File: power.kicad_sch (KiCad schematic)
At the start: 55 parts, among them J3 Conn_02x02_Counter_Clockwise, Q3 Q_NMOS, Q4 Q_NMOS, Q5 Q_NMOS, Q6 Q_NMOS, U10 CJ431, U6 TPS5430DDA, U7 TPS56A37, U8 TPS2121, U9 LDL212PV33R

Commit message: schem: add title
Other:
- company: (none) -> Rémi Ait-Younes
- title: (none) -> Motor Power POC
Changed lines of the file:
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@@
 	(generator_version "9.0")
 	(paper "A4")
+	(title_block
+		(title "Motor Power POC")
+		(date "2025-11-30")
+		(rev "01")
+		(company "Rémi Ait-Younes")
+	)
 	(rectangle
 		(start 246.38 93.98)

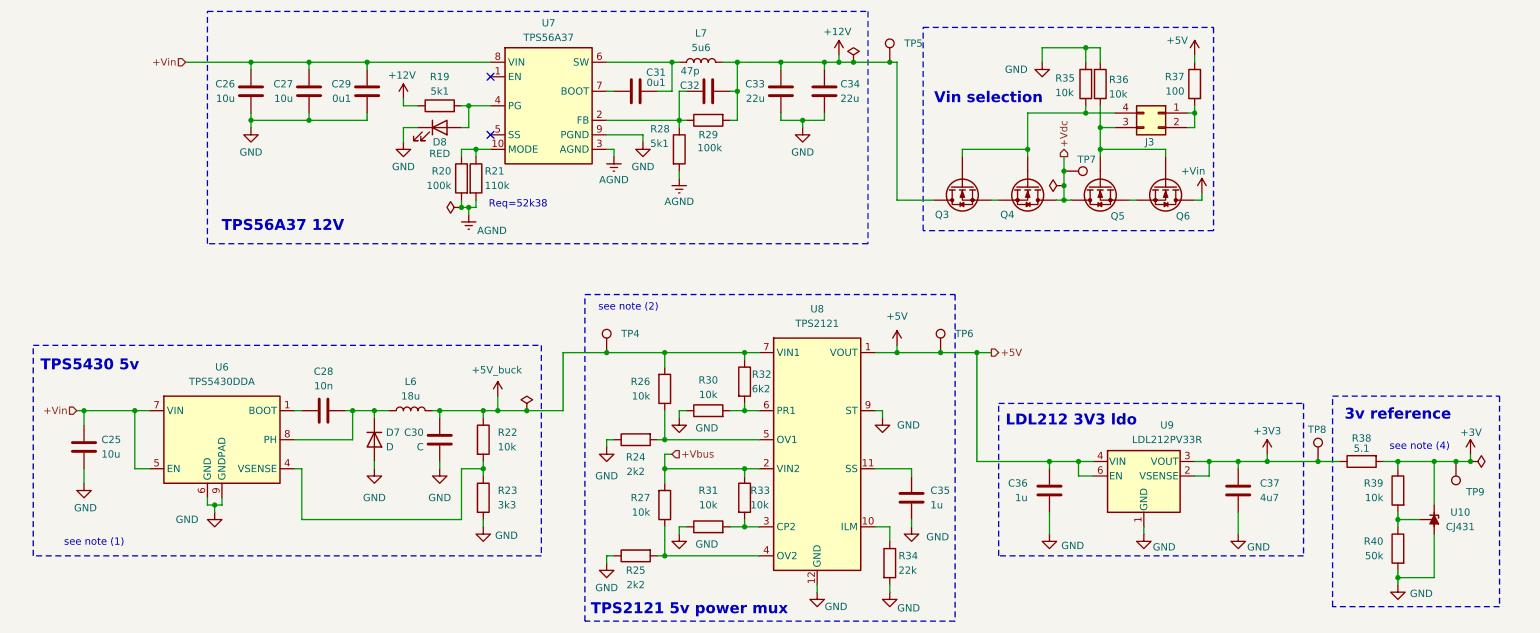
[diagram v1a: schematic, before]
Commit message: schem: assign footprints
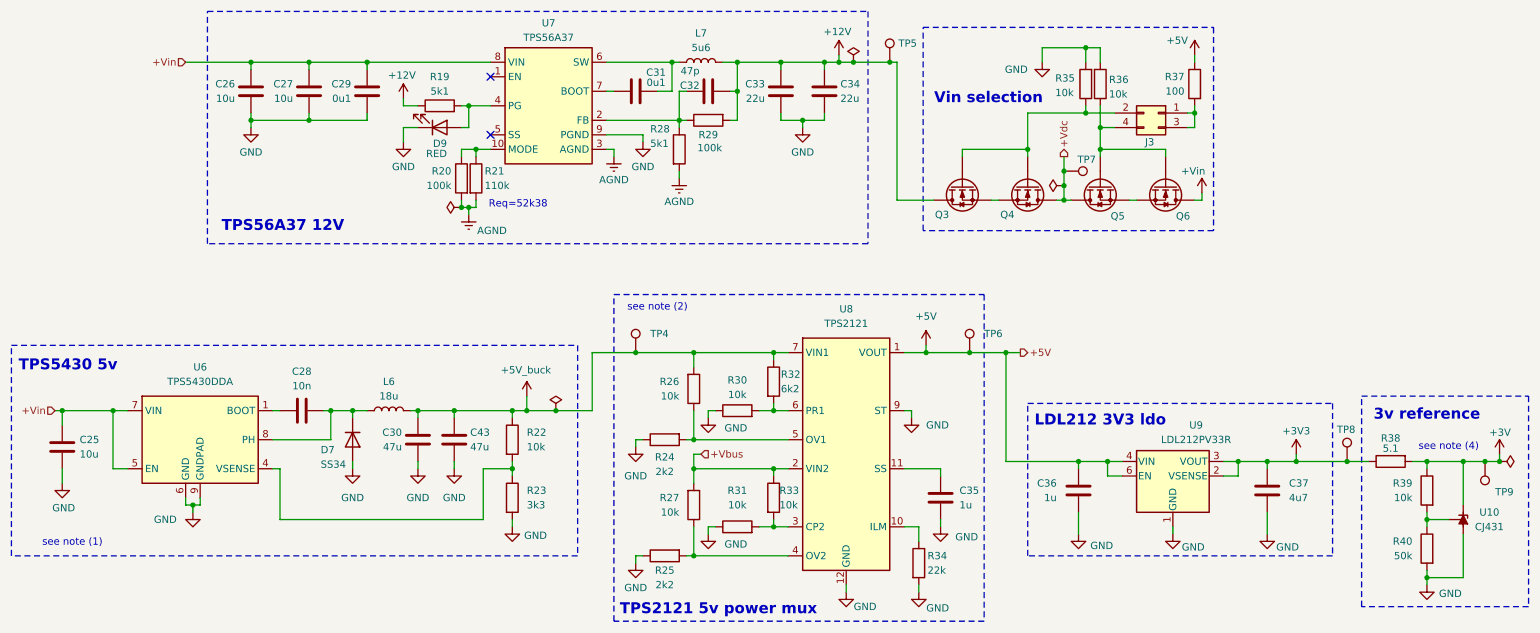
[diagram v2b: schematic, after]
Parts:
- removed D8: RED, symbol Device:LED
- added C43: 47u, Capacitor_SMD:C_1206_3216Metric, symbol Device:C
- added D9: RED, LED_SMD:LED_0603_1608Metric, symbol Device:LED
- C25, C26, C27, C33, C34: footprint (none) -> Capacitor_SMD:C_0805_2012Metric
- C28, C29, C31, C32, C35, C36, C37: footprint (none) -> Capacitor_SMD:C_0402_1005Metric
- C30: value C -> 47u; footprint (none) -> Capacitor_SMD:C_1206_3216Metric
- D7: value D -> SS34; footprint (none) -> Diode_SMD:D_SMA
- J3: footprint (none) -> Connector_PinHeader_2.54mm:PinHeader_2x02_P2.54mm_Vertical; symbol Connector_Generic:Conn_02x02_Counter_Clockwise -> Connector_Generic:Conn_02x02_Odd_Even
- Q3, Q4, Q5, Q6: footprint (none) -> Package_SO:Vishay_PowerPAK_1212-8_Single
- R19, R20, R22, R23, R24, R25, R26, R27, R28, R29, R30, R31, R32, R33, R34, R35, R36: footprint (none) -> Resistor_SMD:R_0402_1005Metric
- R21, R37: footprint (none) -> Resistor_SMD:R_0603_1608Metric
- TP4, TP5, TP6, TP7, TP8, TP9: footprint (none) -> GLCS:TestPoint_Keystone_5015_Micro_Mini
- U7: footprint (none) -> GLCS:Texas_RPA0010A_VQFN-HR-10_3x3mm_P0.5mm
- U9: footprint Pers:DFN-6-1EP_2x2mm_P0.5mm_ST -> GLCS:DFN-6-1EP_2x2mm_P0.5mm_ST; symbol Pers:LDL212PV33R -> GLCS:LDL212PV33R
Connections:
- net +5V_buck: now also C43.1
- net GND: now also C43.2, D9.1 (K)
- net at R19.2, U7.4 (PG): now also D9.2 (A)
- net at J3.1 (Pin_1), R37.2: now also J3.3 (Pin_3); no longer J3.2 (Pin_2)
- net at Q5.G, Q6.G, R36.1: now also J3.4 (Pin_4); no longer J3.3 (Pin_3)
- net at Q3.G, Q4.G, R35.1: now also J3.2 (Pin_2); no longer J3.4 (Pin_4)
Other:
- moved on the sheet: C25, C28, C35, C36, C37, D7, L6, R22, R23, R24, R25, R26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

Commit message: schem: add ordering info to BOM
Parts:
- C25, C26, C27: Basic (none) -> Y; JLCPCB Part # (none) -> C440198; Manufacturer (none) -> Murata; Manufacturer Part Number (none) -> GRM21BR61H106KE43L
- C28: Basic (none) -> Y; JLCPCB Part # (none) -> C15195; Manufacturer (none) -> Samsung Electro-Mechanics; Manufacturer Part Number (none) -> CL05B103KB5NNNC
- C29, C31: Basic (none) -> Y; JLCPCB Part # (none) -> C307331; Manufacturer (none) -> Samsung Electro-Mechanics; Manufacturer Part Number (none) -> CL05B104KB54PNC
- C30, C43: Basic (none) -> Y; JLCPCB Part # (none) -> C96123; Manufacturer (none) -> Samsung Electro-Mechanics; Manufacturer Part Number (none) -> CL31A476MPHNNNE
- C32: Basic (none) -> Y; JLCPCB Part # (none) -> C1567; Manufacturer (none) -> Guangdong Fenghua Advanced Tech (FH); Manufacturer Part Number (none) -> 0402CG470J500NT
- C33, C34: Basic (none) -> Y; JLCPCB Part # (none) -> C45783; Manufacturer (none) -> Samsung Electro-Mechanics; Manufacturer Part Number (none) -> CL21A226MAQNNNE
- C35, C36: Basic (none) -> Y; JLCPCB Part # (none) -> C52923; Manufacturer (none) -> Samsung Electro-Mechanics; Manufacturer Part Number (none) -> CL05A105KA5NQNC
- C37: Basic (none) -> Y; JLCPCB Part # (none) -> C23733; Manufacturer (none) -> Samsung Electro-Mechanics; Manufacturer Part Number (none) -> CL05A475MP5NRNC
- D7: Basic (none) -> Y; JLCPCB Part # (none) -> C8678; Manufacturer (none) -> Microdiode Semiconductor (MDD); Manufacturer Part Number (none) -> SS34
- J3: now left out of the parts list
- L6: footprint (none) -> Inductor_SMD:L_Sunlord_SWRB1207S; Basic (none) -> X; JLCPCB Part # (none) -> C73501; Manufacturer (none) -> Sunlord; Manufacturer Part Number (none) -> SWRH1207B-180MT
- L7: footprint (none) -> Inductor_SMD:L_Sunlord_MWSA0804S; Basic (none) -> X; JLCPCB Part # (none) -> C17700168; Manufacturer (none) -> Sunlord; Manufacturer Part Number (none) -> MWSA0804S-5R6MT
- Q3, Q4, Q5, Q6: Basic (none) -> X; JLCPCB Part # (none) -> C111309; Manufacturer (none) -> Vishay Intertech; Manufacturer Part Number (none) -> SIS412DN-T1-GE3
- R19, R28: Basic (none) -> Y; JLCPCB Part # (none) -> C25905; Manufacturer (none) -> Uniroyal Elec; Manufacturer Part Number (none) -> 0402WGF5101TCE
- R20, R29: Basic (none) -> Y; JLCPCB Part # (none) -> C25741; Manufacturer (none) -> Uniroyal Elec; Manufacturer Part Number (none) -> 0402WGF1003TCE
- R21: Basic (none) -> E; JLCPCB Part # (none) -> C25805; Manufacturer (none) -> Uniroyal Elec; Manufacturer Part Number (none) -> 0603WAF1103T5E
- R22, R26, R27, R30, R31, R33, R35, R36: Basic (none) -> Y; JLCPCB Part # (none) -> C25744; Manufacturer (none) -> Uniroyal Elec; Manufacturer Part Number (none) -> 0402WGF1002TCE
- R23: Basic (none) -> Y; JLCPCB Part # (none) -> C25890; Manufacturer (none) -> Uniroyal Elec; Manufacturer Part Number (none) -> 0402WGF3301TCE
- R24, R25: Basic (none) -> Y; JLCPCB Part # (none) -> C25879; Manufacturer (none) -> Uniroyal Elec; Manufacturer Part Number (none) -> 0402WGF2201TCE
- R32: footprint Resistor_SMD:R_0402_1005Metric -> Resistor_SMD:R_0603_1608Metric; Basic (none) -> Y; JLCPCB Part # (none) -> C4260; Manufacturer (none) -> Uniroyal Elec; Manufacturer Part Number (none) -> 0603WAF6201T5E
- R34: Basic (none) -> Y; JLCPCB Part # (none) -> C25768; Manufacturer (none) -> Uniroyal Elec; Manufacturer Part Number (none) -> 0402WGF2202TCE
- R37: Basic (none) -> Y; JLCPCB Part # (none) -> C22775; Manufacturer (none) -> Uniroyal Elec; Manufacturer Part Number (none) -> 0603WAF1000T5E
- TP4, TP5, TP6, TP7, TP8, TP9: Basic (none) -> X; JLCPCB Part # (none) -> C2906768; Manufacturer (none) -> Keystone; Manufacturer Part Number (none) -> 5015
- U6: Basic (none) -> Y; JLCPCB Part # (none) -> C9864; Manufacturer (none) -> Texas Instruments; Manufacturer Part Number (none) -> TPS5430DDAR
- U7: Basic (none) -> X; JLCPCB Part # (none) -> C22392669; Manufacturer (none) -> Texas Instruments; Manufacturer Part Number (none) -> TPS56A37RPAR
- U8: Basic (none) -> X; JLCPCB Part # (none) -> C485916; Manufacturer (none) -> Texas Instruments; Manufacturer Part Number (none) -> TPS2121RUXR
- U9: Basic (none) -> X; JLCPCB Part # (none) -> C2969892; Manufacturer (none) -> STMicroelectronics; Manufacturer Part Number (none) -> LDL212PV33R

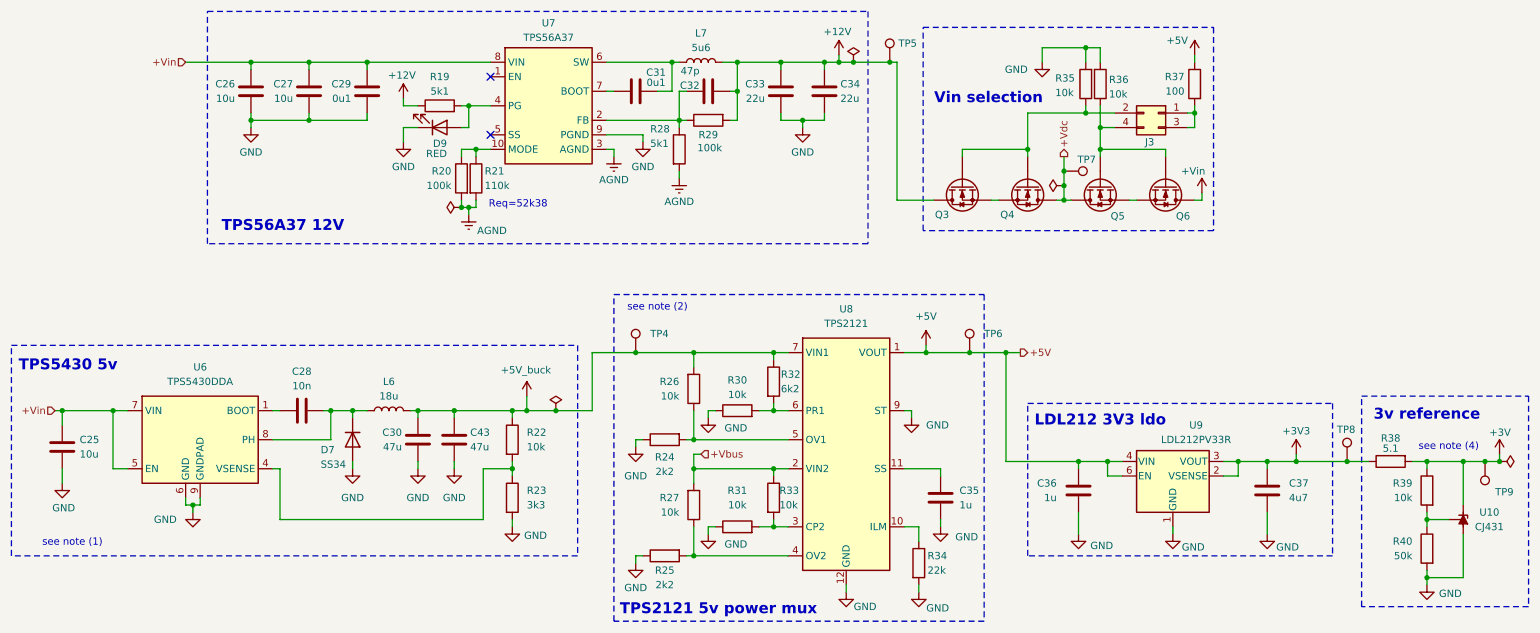
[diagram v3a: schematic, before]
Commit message: schem: renumber
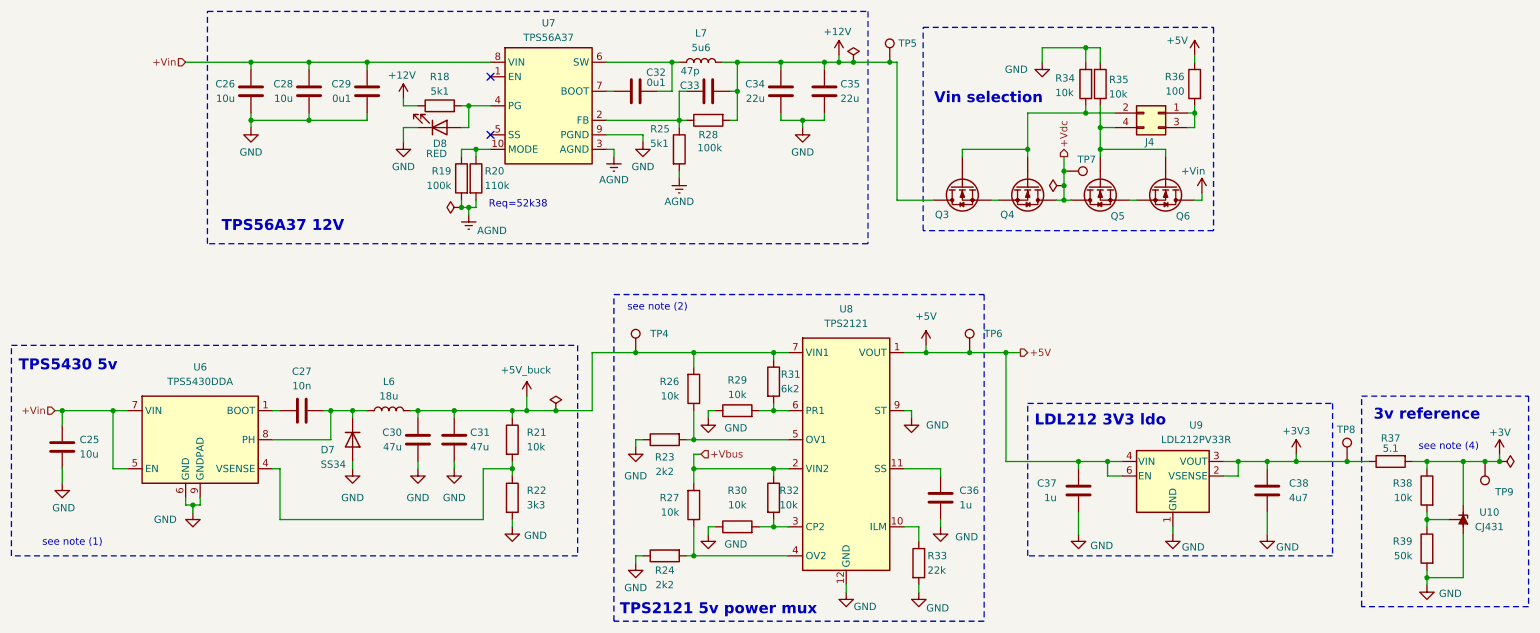
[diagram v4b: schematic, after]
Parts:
- renumbered C28 to C27, C27 to C28, C43 to C31, C31 to C32, C32 to C33, C33 to C34, C34 to C35, C35 to C36, C36 to C37, C37 to C38, D9 to D8, J3 to J4, R19 to R18, R20 to R19, R21 to R20, R22 to R21, R23 to R22, R24 to R23, R25 to R24, R28 to R25, R29 to R28, R30 to R29, R31 to R30, R32 to R31, R33 to R32, R34 to R33, R35 to R34, R36 to R35, R37 to R36, R38 to R37, R39 to R38, R40 to R39

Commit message: schem: update MOSFETs symbol
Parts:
- Q3, Q4, Q5, Q6: symbol Device:Q_NMOS -> Transistor_FET:SiS415DNT
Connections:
- net +12V: now also Q3.1 (S), Q3.2 (S), Q3.3 (S); no longer Q3.D
- net +Vdc: now also Q4.1 (S), Q4.2 (S), Q4.3 (S), Q5.1 (S), Q5.2 (S), Q5.3 (S); no longer Q4.D, Q5.D
- net +Vin: now also Q6.1 (S), Q6.2 (S), Q6.3 (S); no longer Q6.D
- net at J4.4 (Pin_4), R35.1: now also Q5.4 (G), Q6.4 (G); no longer Q5.G, Q6.G
- net at J4.2 (Pin_2), R34.1: now also Q3.4 (G), Q4.4 (G); no longer Q3.G, Q4.G
- new net: Q5.5 (D), Q6.5 (D)
- new net: Q3.5 (D), Q4.5 (D)
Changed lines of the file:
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@@
 	)
 	(symbol
-		(lib_id "Device:Q_NMOS")
-		(at 205.74 57.15 90)
-		(mirror x)
+		(lib_id "Transistor_FET:SiS415DNT")
+		(at 205.74 57.15 270)
 		(unit 1)
 		(exclude_from_sim no)
@@
 		(dnp no)
 		(property "Reference" "Q5"
-			(at 208.788 62.484 90)
+			(at 202.692 62.484 90)
 			(effects
 				(font
@@
 		)
 		(property "Footprint" "Package_SO:Vishay_PowerPAK_1212-8_Single"
-			(at 203.2 62.23 0)
+			(at 208.28 62.23 0)
 			(effects
 				(font
@@
 			)
 		)
-		(pin "S"
-		)
-		(pin "G"
-		)
-		(pin "D"
+		(pin "3"
+		)
+		(pin "4"
+		)
+		(pin "2"
+		)
+		(pin "5"
+		)
+		(pin "1"
 		)
 		(instances
@@
 	)
 	(symbol
-		(lib_id "Device:Q_NMOS")
-		(at 181.61 57.15 90)
-		(mirror x)
+		(lib_id "Transistor_FET:SiS415DNT")
+		(at 181.61 57.15 270)
 		(unit 1)
 		(exclude_from_sim no)
@@
 		(dnp no)
 		(property "Reference" "Q3"
-			(at 178.054 62.23 90)
+			(at 185.166 62.23 90)
 			(effects
 				(font
@@
 		)
 		(property "Footprint" "Package_SO:Vishay_PowerPAK_1212-8_Single"
-			(at 179.07 62.23 0)
+			(at 184.15 62.23 0)
 			(effects
 				(font
@@
 			)
 		)
-		(pin "S"
-		)
-		(pin "G"
-		)
-		(pin "D"
+		(pin "3"
+		)
+		(pin "4"
+		)
+		(pin "2"
+		)
+		(pin "5"
+		)
+		(pin "1"
 		)
 		(instances
@@
 	)
 	(symbol
-		(lib_id "Device:Q_NMOS")
-		(at 193.04 57.15 270)
+		(lib_id "Transistor_FET:SiS415DNT")
+		(at 193.04 57.15 90)
+		(mirror x)
 		(unit 1)
 		(exclude_from_sim no)
@@
 		(dnp no)
 		(property "Reference" "Q4"
-			(at 189.484 62.23 90)
+			(at 196.596 62.23 90)
 			(effects
 				(font
@@
 		)
 		(property "Footprint" "Package_SO:Vishay_PowerPAK_1212-8_Single"
-			(at 195.58 62.23 0)
+			(at 190.5 62.23 0)
 			(effects
 				(font
@@
 			)
 		)
-		(pin "S"
-		)
-		(pin "G"
-		)
-		(pin "D"
+		(pin "5"
+		)
+		(pin "3"
+		)
+		(pin "4"
+		)
+		(pin "1"
+		)
+		(pin "2"
 		)
 		(instances
@@
 	)
 	(symbol
-		(lib_id "Device:Q_NMOS")
-		(at 217.17 57.15 270)
+		(lib_id "Transistor_FET:SiS415DNT")
+		(at 217.17 57.15 90)
+		(mirror x)
 		(unit 1)
 		(exclude_from_sim no)
@@
 		(dnp no)
 		(property "Reference" "Q6"
-			(at 220.218 62.484 90)
+			(at 214.122 62.484 90)
 			(effects
 				(font
@@
 		)
 		(property "Footprint" "Package_SO:Vishay_PowerPAK_1212-8_Single"
-			(at 219.71 62.23 0)
+			(at 214.63 62.23 0)
 			(effects
 				(font
@@
 			)
 		)
-		(pin "S"
-		)
-		(pin "G"
-		)
-		(pin "D"
-		)
-		(instances
+		(pin "5"
+		)
+		(pin "3"
+		)
+		(pin "4"
+		)
+		(pin "1"
+		)
+		(pin "2"
+		)
+		(instances

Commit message: schem: update MOSFETs footprints to correct N-channel
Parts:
- Q3, Q4, Q5, Q6: symbol Transistor_FET:SiS415DNT -> Transistor_FET:SiS454DN
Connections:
- net +12V: now also Q3.5 (D); no longer Q3.1 (S), Q3.2 (S), Q3.3 (S)
- net +Vdc: now also Q4.5 (D), Q5.5 (D); no longer Q4.1 (S), Q4.2 (S), Q4.3 (S), Q5.1 (S), Q5.2 (S), Q5.3 (S)
- net +Vin: now also Q6.5 (D); no longer Q6.1 (S), Q6.2 (S), Q6.3 (S)
- new net: Q5.1 (S), Q5.2 (S), Q5.3 (S), Q6.1 (S), Q6.2 (S), Q6.3 (S)
- new net: Q3.1 (S), Q3.2 (S), Q3.3 (S), Q4.1 (S), Q4.2 (S), Q4.3 (S)
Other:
- moved on the sheet: Q3, Q4, Q5, Q6
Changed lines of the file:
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@@
 	)
 	(symbol
-		(lib_id "Transistor_FET:SiS415DNT")
-		(at 205.74 57.15 270)
+		(lib_id "Transistor_FET:SiS454DN")
+		(at 205.74 57.15 90)
+		(mirror x)
 		(unit 1)
 		(exclude_from_sim no)
@@
 		(dnp no)
 		(property "Reference" "Q5"
-			(at 202.692 62.484 90)
+			(at 208.788 62.484 90)
 			(effects
 				(font
@@
 		)
 		(property "Footprint" "Package_SO:Vishay_PowerPAK_1212-8_Single"
-			(at 208.28 62.23 0)
+			(at 203.2 62.23 0)
 			(effects
 				(font
@@
 	)
 	(symbol
-		(lib_id "Transistor_FET:SiS415DNT")
-		(at 181.61 57.15 270)
+		(lib_id "Transistor_FET:SiS454DN")
+		(at 181.61 57.15 90)
+		(mirror x)
 		(unit 1)
 		(exclude_from_sim no)
@@
 		(dnp no)
 		(property "Reference" "Q3"
-			(at 185.166 62.23 90)
+			(at 178.054 62.23 90)
 			(effects
 				(font
@@
 		)
 		(property "Footprint" "Package_SO:Vishay_PowerPAK_1212-8_Single"
-			(at 184.15 62.23 0)
+			(at 179.07 62.23 0)
 			(effects
 				(font
@@
 	)
 	(symbol
-		(lib_id "Transistor_FET:SiS415DNT")
-		(at 193.04 57.15 90)
-		(mirror x)
+		(lib_id "Transistor_FET:SiS454DN")
+		(at 193.04 57.15 270)
 		(unit 1)
 		(exclude_from_sim no)
@@
 		(dnp no)
 		(property "Reference" "Q4"
-			(at 196.596 62.23 90)
+			(at 189.484 62.23 90)
 			(effects
 				(font
@@
 		)
 		(property "Footprint" "Package_SO:Vishay_PowerPAK_1212-8_Single"
-			(at 190.5 62.23 0)
+			(at 195.58 62.23 0)
 			(effects
 				(font
@@
 	)
 	(symbol
-		(lib_id "Transistor_FET:SiS415DNT")
-		(at 217.17 57.15 90)
-		(mirror x)
+		(lib_id "Transistor_FET:SiS454DN")
+		(at 217.17 57.15 270)
 		(unit 1)
 		(exclude_from_sim no)
@@
 		(dnp no)
 		(property "Reference" "Q6"
-			(at 214.122 62.484 90)
+			(at 220.218 62.484 90)
 			(effects
 				(font
@@
 		)
 		(property "Footprint" "Package_SO:Vishay_PowerPAK_1212-8_Single"
-			(at 214.63 62.23 0)
-			(effects
-				(font
+			(at 219.71 62.23 0)
+			(effects
+				(font
